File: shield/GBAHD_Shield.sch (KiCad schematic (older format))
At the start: 17 parts, among them J1 Conn_01x40, J2 Conn_02x08_Top_Bottom, J3 Conn_01x16, J4 Conn_02x10_Top_Bottom, J5 Conn_01x05, J6 Conn_02x03_Odd_Even, J7 Conn_01x01, SW1 SW_Push, U1 SNES_7PIN, U2 ATmega328P-AU, U3 WAS3157B, X1 Crystal_GND2

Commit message: Updated shield PCB and readme
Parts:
- removed C2: 22pF, Capacitor_SMD:C_0805_2012Metric_Pad1.18x1.45mm_HandSolder, symbol Device:C
- removed J5: Conn_01x05, OFFSET:Pads_01x05, symbol Connector_Generic:Conn_01x05
- removed U3: WAS3157B, OFFSET:SOT-363, symbol Raizu:WAS3157B
- removed X1: Crystal_GND2, Crystal:Crystal_SMD_3225-4Pin_3.2x2.5mm, symbol Device:Crystal_GND24
- added C4: 22u, Capacitor_SMD:C_0805_2012Metric_Pad1.18x1.45mm_HandSolder, symbol Device:C
- added J10, J11, J12, J13, J15, J16, J18, J5: Conn_01x01, TestPoint:TestPoint_Pad_1.5x1.5mm, symbol Connector_Generic:Conn_01x01
- added J9: FLEX_GBA-SP, Connector_FFC-FPC:TE_3-1734839-4_1x34-1MP_P0.5mm_Horizontal, symbol Connector_Generic:Conn_01x34
- added Q1: Q_PMOS_GSD, Package_TO_SOT_SMD:SOT-23, symbol Device:Q_PMOS_GSD
- added R2, R3: 10K, Resistor_SMD:R_0805_2012Metric_Pad1.20x1.40mm_HandSolder, symbol Device:R
- added R4: 16.2K, Resistor_SMD:R_0805_2012Metric_Pad1.20x1.40mm_HandSolder, symbol Device:R
- added R5: 7.5K, Resistor_SMD:R_0805_2012Metric_Pad1.20x1.40mm_HandSolder, symbol Device:R
- added SJ2: SOLDER_JUMPER, Jumper:SolderJumper-2_P1.3mm_Open_RoundedPad1.0x1.5mm, symbol GBAHD_Shield-rescue:SOLDER_JUMPER-keyboard_parts
- added U3, U4: 74HC595, Package_SO:TSSOP-16_4.4x5mm_P0.65mm, symbol 74xx:74HC595
- added U5: AMS1117, Package_TO_SOT_SMD:SOT-223-3_TabPin2, symbol Regulator_Linear:AMS1117
- C1: value 22pF -> 100nF
- J1: value Conn_01x40 -> FFC_OGBA; footprint OFFSET:JUSHUO_AFC07-S40FCC-00 -> Connector_FFC-FPC:TE_4-1734839-0_1x40-1MP_P0.5mm_Horizontal
- J3: footprint OFFSET:JUSHUO_AFC07-S16FCC-00 -> Connector_FFC-FPC:TE_1-1734839-6_1x16-1MP_P0.5mm_Horizontal
- J7: footprint OFFSET:SOLDER_PAD -> TestPoint:TestPoint_Pad_1.5x1.5mm
- SJ1: symbol keyboard_parts:SOLDER_JUMPER -> GBAHD_Shield-rescue:SOLDER_JUMPER-keyboard_parts
- U1: symbol Raizu:SNES_7PIN -> GBAHD_Shield-rescue:SNES_7PIN-Raizu
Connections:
- net labels added: +5V, PIXEL_GRID, QH_OUT-SER_IN, RX, TX, VCC
- net labels removed: SP_3V3, SP_ARD15
- wire segments 49 -> 210
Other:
- note added: "GBA Audio"
- note added: "GBA Buttons Serial-to-Parallel"
- note added: "GBA Display"
- note added: "GBA Display Connectors"
- note added: "GBA FFC-Connector"
- note added: "GBA ISR/Power Supply"
- note added: "ICSP"
- note added: "Idea by: sanchezand"
- note added: "Microcontroller"
- note added: "Power-Supply"
- note added: "Reset Button"
- note added: "SNES Controller Connector"
- note added: "SNES Data"
- note added: "Shield Connector"
- note added: "Signal Connections"
- note added: "UART"
- note added: "gbaHD\nShield"
- note added: "~4.2~/3.3"
- moved on the sheet: C3, J1, J2, J3, J4, J6, J7, R1, SW1, U2

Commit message: Updated to "Full-Shield"
* changed supplies to 3V3 and 4V0
* added pads for BAT connection
* added 32-Pin FFC Connector
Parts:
- removed J2: Conn_02x08_Top_Bottom, Connector_PinHeader_2.54mm:PinHeader_2x08_P2.54mm_Vertical, symbol Connector_Generic:Conn_02x08_Odd_Even
- removed J4: Conn_02x10_Top_Bottom, Connector_PinHeader_2.54mm:PinHeader_2x10_P2.54mm_Vertical, symbol Connector_Generic:Conn_02x10_Odd_Even
- removed R3: 10K, Resistor_SMD:R_0805_2012Metric_Pad1.20x1.40mm_HandSolder, symbol Device:R
- removed R4: 16.2K, Resistor_SMD:R_0805_2012Metric_Pad1.20x1.40mm_HandSolder, symbol Device:R
- removed R5: 7.5K, Resistor_SMD:R_0805_2012Metric_Pad1.20x1.40mm_HandSolder, symbol Device:R
- removed SJ2: SOLDER_JUMPER, Jumper:SolderJumper-2_P1.3mm_Open_RoundedPad1.0x1.5mm, symbol GBAHD_Shield-rescue:SOLDER_JUMPER-keyboard_parts
- removed U5: AMS1117, Package_TO_SOT_SMD:SOT-223-3_TabPin2, symbol Regulator_Linear:AMS1117
- added BAT+1, BAT-1: Conn_01x01, TestPoint:TestPoint_Pad_1.5x1.5mm, symbol Connector_Generic:Conn_01x01
- added J10, J8: Conn_01x10, Connector_PinHeader_2.54mm:PinHeader_1x10_P2.54mm_Vertical, symbol Connector_Generic:Conn_01x10
- added J2: FFC_OGBA_32, Connector_FFC-FPC:TE_3-1734839-2_1x32-1MP_P0.5mm_Horizontal, symbol Connector_Generic:Conn_01x32
- added J6: Conn_01x06, Connector_PinHeader_2.54mm:PinHeader_1x06_P2.54mm_Vertical, symbol Connector_Generic:Conn_01x06
- added J7, J9: Conn_01x08, Connector_PinHeader_2.54mm:PinHeader_1x08_P2.54mm_Vertical, symbol Connector_Generic:Conn_01x08
- added JP1: SolderJumper_3_Open, Jumper:SolderJumper-3_P1.3mm_Open_Pad1.0x1.5mm_NumberLabels, symbol Jumper:SolderJumper_3_Open
- added R1: 2.2k, Resistor_SMD:R_0805_2012Metric_Pad1.20x1.40mm_HandSolder, symbol Device:R
- added R2: 1k, Resistor_SMD:R_0805_2012Metric_Pad1.20x1.40mm_HandSolder, symbol Device:R
- added U1: AZ1117R-ADJ, Package_TO_SOT_SMD:SOT-89-3, symbol Regulator_Linear:AZ1117R-ADJ
- J3: renamed from J9; value FLEX_GBA-SP -> FFC_GBA-SP
- J5: renamed from J1; value FFC_OGBA -> FFC_OGBA_40
- SJ1: footprint Jumper:SolderJumper-2_P1.3mm_Open_RoundedPad1.0x1.5mm -> Jumper:SolderJumper-2_P1.3mm_Open_TrianglePad1.0x1.5mm
- SW1: footprint OFFSET:XKB-TS-1185EC-C-D-B -> Button_Switch_SMD:SW_Push_1P1T_NO_CK_KMR2
- U2: renamed from U3; footprint Package_SO:TSSOP-16_4.4x5mm_P0.65mm -> Package_SO:SOIC-16_3.9x9.9mm_P1.27mm
- U3: renamed from U4; footprint Package_SO:TSSOP-16_4.4x5mm_P0.65mm -> Package_SO:SOIC-16_3.9x9.9mm_P1.27mm
- renumbered C4 to C2, J7 to J1, J6 to J11, J3 to J4, R2 to R3, R1 to R4, J15 to T1, J10 to T2, J16 to T3, J11 to T4, J12 to T5, J18 to T6, J13 to T7, J5 to T8, U1 to U4, U2 to U5
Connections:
- net +5V: now also J7.4 (Pin_4), U1.3 (VI)
- net GBA_AUD1: now also J9.3 (Pin_3)
- net GBA_AUD2: now also J9.4 (Pin_4)
- net GBA_CLK: now also J8.9 (Pin_9)
- net GBA_VCC: now also BAT+1.1 (Pin_1)
- net GB_B1: now also J2.22 (Pin_22), J8.2 (Pin_2)
- net GB_B2: now also J2.21 (Pin_21), J9.6 (Pin_6)
- net GB_B3: now also J2.20 (Pin_20), J8.3 (Pin_3)
- net GB_B4: now also J2.19 (Pin_19), J9.7 (Pin_7)
- net GB_B5: now also J2.18 (Pin_18), J8.4 (Pin_4)
- net GB_DCLK: now also J2.2 (Pin_2), J8.10 (Pin_10)
- net GB_G1: now also J2.16 (Pin_16), J9.8 (Pin_8)
- net GB_G2: now also J2.15 (Pin_15), J8.5 (Pin_5)
- net GB_G3: now also J10.1 (Pin_1), J2.14 (Pin_14)
- net GB_G4: now also J2.13 (Pin_13), J8.6 (Pin_6)
- net GB_G5: now also J10.2 (Pin_2), J2.12 (Pin_12)
- net GB_R1: now also J2.11 (Pin_11), J8.7 (Pin_7)
- net GB_R2: now also J10.3 (Pin_3), J2.10 (Pin_10)
- net GB_R3: now also J2.9 (Pin_9), J8.8 (Pin_8)
- net GB_R4: now also J10.4 (Pin_4), J2.8 (Pin_8)
- net GB_R5: now also J10.6 (Pin_6), J2.7 (Pin_7)
- net GB_SPS: now also J2.25 (Pin_25), J8.1 (Pin_1)
- net GND: now also BAT-1.1 (Pin_1), J10.7 (Pin_7), J2.17 (Pin_17), J7.2 (Pin_2), J7.3 (Pin_3), R1.1
- net PIXEL_GRID: now also J9.5 (Pin_5)
- net RX: now also J9.1 (Pin_1)
- net SP_ARD1: now also J9.2 (Pin_2)
- net SP_ARD12: now also J10.5 (Pin_5)
- net VCC: now also JP1.2 (C); no longer C2.2
- new net: R1.2, R2.1, U1.1 (ADJ)
- new net +3V3: J7.5 (Pin_5), JP1.1 (A)
- new net +4V: C2.2, JP1.3 (B), R2.2, U1.2 (VO)
- new net AR_A0: J6.1 (Pin_1)
- new net AR_A1: J6.2 (Pin_2)
- new net AR_A2: J6.3 (Pin_3)
- new net AR_A3: J6.4 (Pin_4)
- new net AR_A4: J6.5 (Pin_5)
- new net AR_A5: J6.6 (Pin_6)
- new net SP_ARRES: J7.6 (Pin_6)
- new net SP_ARSCL: J10.10 (Pin_10)
- new net SP_ARSDA: J10.9 (Pin_9)
- new net SP_VIN: J7.1 (Pin_1)
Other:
- note added: "optional battery connector"
- note removed: "~4.2~/3.3"
- moved on the sheet: C1, C2, J3, J5, Q1, R3, U4

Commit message: Major Updates
* Added QSB for GBA SP
* Fixed wrong supply voltare for Components in case of SP setup
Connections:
- net +3V3: now also C3.2, J11.2 (Pin_2), R4.1, U2.10 (~SRCLR), U2.16 (VCC), U3.10 (~SRCLR), U3.16 (VCC), U4.1 (VCC), U5.18 (AVCC), U5.20 (AREF), U5.4 (VCC), U5.6 (VCC)
- net GND: no longer U2.13 (~OE), U3.13 (~OE)
- net VCC: no longer C3.2, J11.2 (Pin_2), R4.1, U2.10 (~SRCLR), U2.16 (VCC), U3.10 (~SRCLR), U3.16 (VCC), U4.1 (VCC), U5.18 (AVCC), U5.20 (AREF), U5.4 (VCC), U5.6 (VCC)
- net ~GBA_BUTTONS_EN~: now reaches U5.13 (PB1)
- net ~GBA_BUTTONS_EN~: now also U2.13 (~OE), U3.13 (~OE)
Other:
- note added: "There might be input clamping here \ndue to 3.3V supply volgate of µC vs. \n4V pullup Voltage.\n\nThis would result in approx. 400µA \ncurrent over the clamping current."
- moved on the sheet: Q1, R3, U2

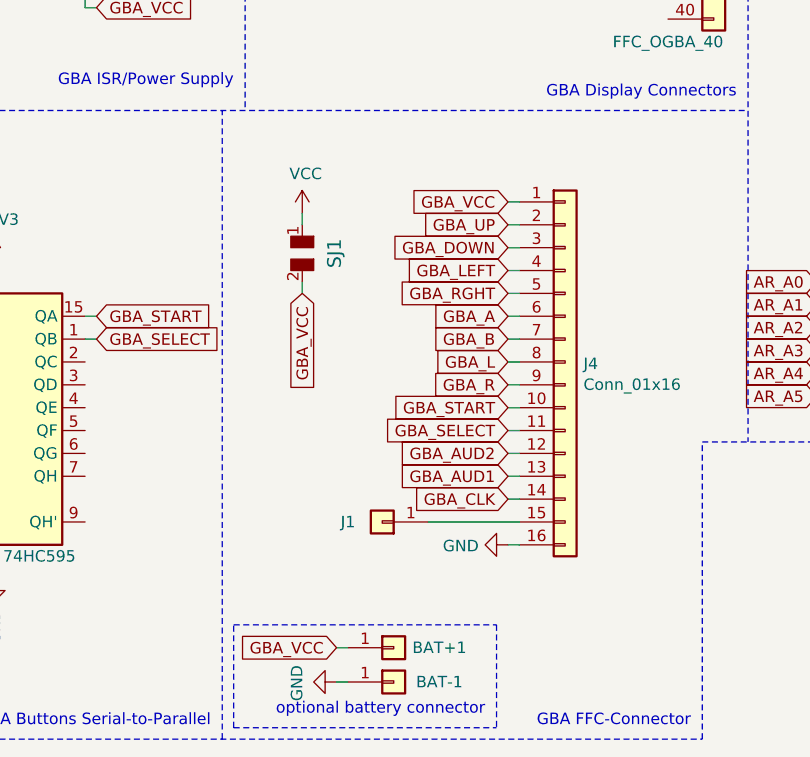
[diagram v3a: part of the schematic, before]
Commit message: some minor changes
* improved SP compatibility
* changed via diameter to 0.6mm and holesize to 0.3mm
* updated Readme
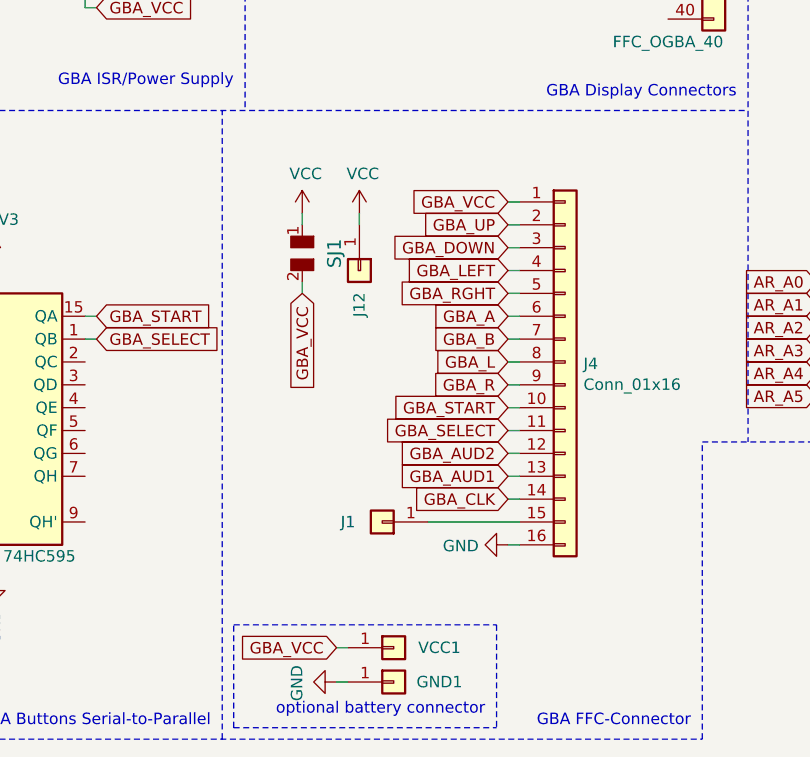
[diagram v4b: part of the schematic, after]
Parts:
- added J12: Conn_01x01, TestPoint:TestPoint_Pad_1.5x1.5mm, symbol Connector_Generic:Conn_01x01
- renumbered BAT-1 to GND1, BAT+1 to VCC1
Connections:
- net VCC: now also J12.1 (Pin_1)
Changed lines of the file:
@@
 Wire Wire Line
 	6050 5500 6100 5500
-Wire Wire Line
-	6100 5400 6050 5400
 Text GLabel 1300 5900 0    50   Input ~ 0
 ICSP_MOSI
@@
 $EndComp
 $Comp
-L Connector_Generic:Conn_01x01 BAT+1
+L Connector_Generic:Conn_01x01 VCC1
 U 1 1 608BF56E
 P 5550 7350
-F 0 "BAT+1" H 5750 7350 50  0000 C CNN
+F 0 "VCC1" H 5750 7350 50  0000 C CNN
 F 1 "Conn_01x01" H 5400 7250 50  0001 C CNN
 F 2 "TestPoint:TestPoint_Pad_1.5x1.5mm" H 5550 7350 50  0001 C CNN
@@
 $EndComp
 $Comp
-L Connector_Generic:Conn_01x01 BAT-1
+L Connector_Generic:Conn_01x01 GND1
 U 1 1 608C02ED
 P 5550 7500
-F 0 "BAT-1" H 5750 7500 50  0000 C CNN
+F 0 "GND1" H 5750 7500 50  0000 C CNN
 F 1 "Conn_01x01" H 5400 7350 50  0001 C CNN
 F 2 "TestPoint:TestPoint_Pad_1.5x1.5mm" H 5550 7500 50  0001 C CNN
@@
 Text GLabel 3350 6500 0    50   Input ~ 0
 ~GBA_BUTTONS_EN~
+$Comp
+L Connector_Generic:Conn_01x01 J12
+U 1 1 607B0906
+P 5400 5700
+F 0 "J12" H 5550 5700 50  0000 C CNN
+F 1 "Conn_01x01" H 5700 5700 50  0001 C CNN
+F 2 "TestPoint:TestPoint_Pad_1.5x1.5mm" H 5400 5700 50  0001 C CNN
+F 3 "~" H 5400 5700 50  0001 C CNN
+	1    5400 5700
+	0    1    1    0
+$EndComp
+$Comp
+L power:VCC #PWR0116
+U 1 1 607E47FD
+P 5400 5450
+F 0 "#PWR0116" H 5400 5300 50  0001 C CNN
+F 1 "VCC" H 5415 5623 50  0000 C CNN
+F 2 "" H 5400 5450 50  0001 C CNN
+F 3 "" H 5400 5450 50  0001 C CNN
+	1    5400 5450
+	1    0    0    -1
+$EndComp
+Wire Wire Line
+	5400 5450 5400 5500
+Wire Wire Line
+	6100 5400 6050 5400
 $EndSCHEMATC

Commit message: updated shield
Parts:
- removed J12, T8: Conn_01x01, TestPoint:TestPoint_Pad_1.5x1.5mm, symbol Connector_Generic:Conn_01x01
- removed SJ1: SOLDER_JUMPER, Jumper:SolderJumper-2_P1.3mm_Open_TrianglePad1.0x1.5mm, symbol GBAHD_Shield-rescue:SOLDER_JUMPER-keyboard_parts
- added D1: RED, LED_SMD:LED_0805_2012Metric_Pad1.15x1.40mm_HandSolder, symbol Device:LED
- added D2: GREEN, LED_SMD:LED_0805_2012Metric_Pad1.15x1.40mm_HandSolder, symbol Device:LED
- added Q2, Q3: Q_NMOS_GSD, Package_TO_SOT_SMD:SOT-23, symbol Device:Q_NMOS_GSD
- added R5: 500, Resistor_SMD:R_0805_2012Metric_Pad1.20x1.40mm_HandSolder, symbol Device:R
- added R6, R7, R8: 10K, Resistor_SMD:R_0805_2012Metric_Pad1.20x1.40mm_HandSolder, symbol Device:R
- T1, T2, T3, T4, T5, T6, T7: footprint TestPoint:TestPoint_Pad_1.5x1.5mm -> TestPoint:TestPoint_Pad_D1.5mm
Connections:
- net GBA_CLK: now also Q3.3 (D); no longer J4.14 (Pin_14)
- net GBA_POWER_SEL: now also Q2.1 (G)
- net GBA_VCC: now also Q2.3 (D), Q3.1 (G), R8.2
- net GND: now also D1.1 (K), D2.1 (K), R5.1, R8.1
- net SP_ARSCL: now also U5.28 (PC5)
- net SP_ARSDA: now also U5.27 (PC4)
- net at T6.1 (Pin_1): now also U5.9 (PD5); no longer U5.10 (PD6)
- net at T7.1 (Pin_1): now also U5.12 (PB0); no longer U5.11 (PD7)
- net at U5.2 (PD4): now also T5.1 (Pin_1)
- net at U5.23 (PC0): now also T1.1 (Pin_1)
- net at U5.24 (PC1): now also T2.1 (Pin_1); no longer T1.1 (Pin_1)
- net at U5.25 (PC2): now also T3.1 (Pin_1); no longer T2.1 (Pin_1)
- net at U5.26 (PC3): now also T4.1 (Pin_1); no longer T3.1 (Pin_1)
- net PIXEL_GRID renamed FPGA_COM
- new net: D1.2 (A), R6.2
- new net: D2.2 (A), R7.2
- new net: Q2.2 (S), R5.2
- new net GBA_CLK': J4.14 (Pin_14), Q3.2 (S)
- new net LED_GREEN: R7.1, U5.11 (PD7)
- new net LED_RED: R6.1, U5.10 (PD6)
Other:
- note added: "Disable clock if GBA is not supplied!"
- note added: "LEDs"
- note removed: "Idea by: sanchezand"
- moved on the sheet: Q1, R3, T1, T2, T3, T5, T6, T7, U2, U3, U4
